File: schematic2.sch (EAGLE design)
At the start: 71 parts, among them IC6 DS3231/SO

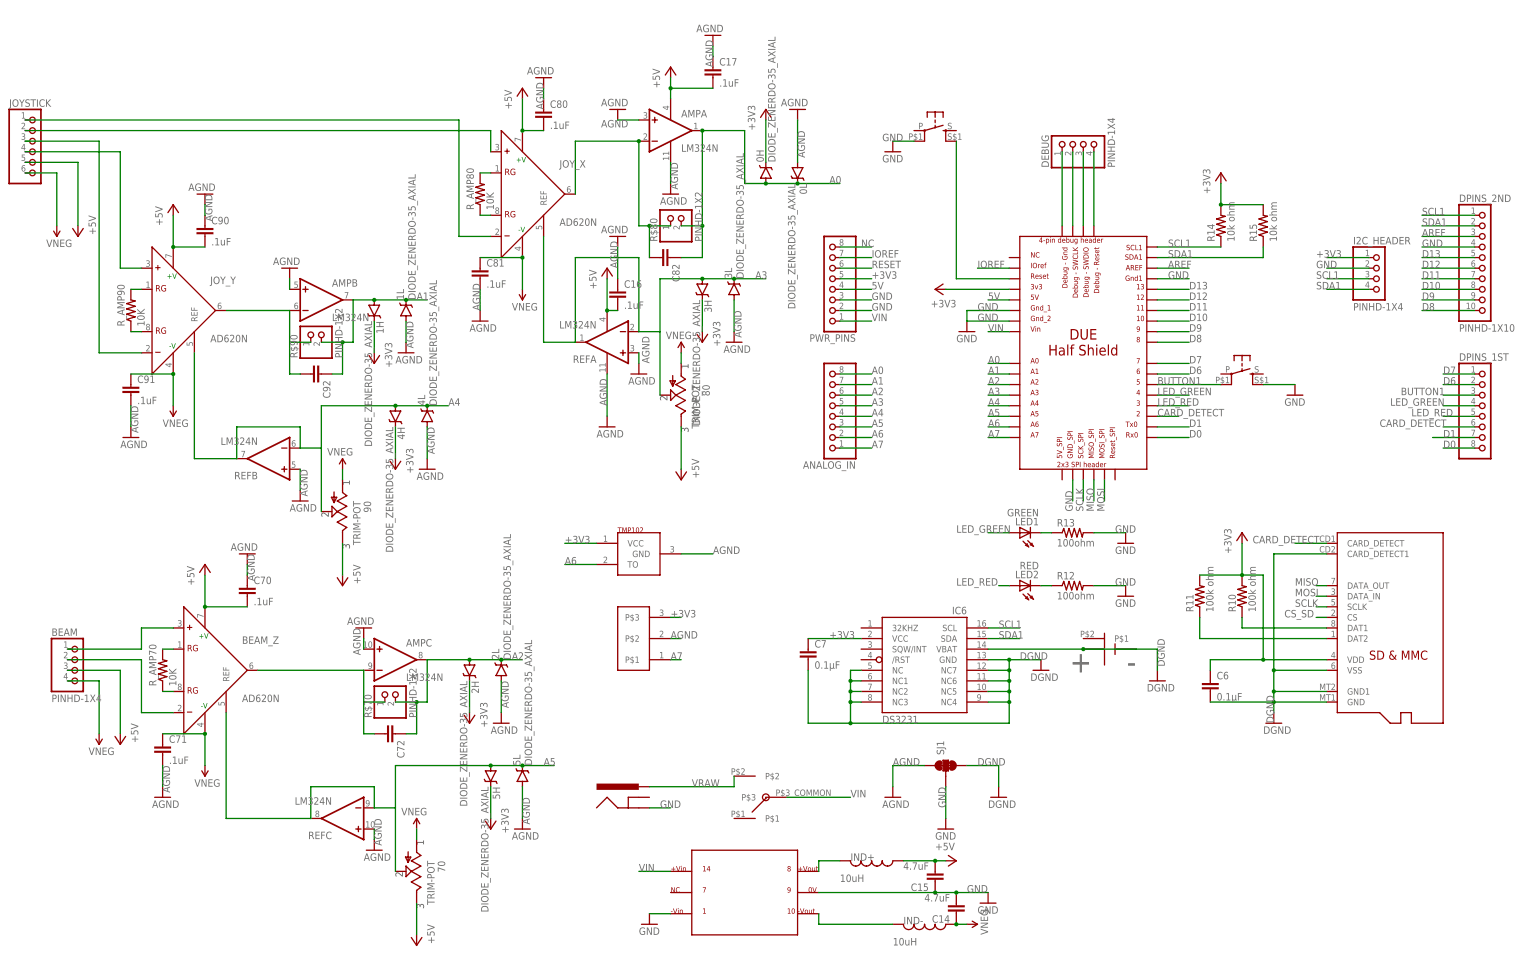
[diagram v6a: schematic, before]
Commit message: Fixed the RC filter arrangement on the 2nd stage op-amps for all three inputs. Move the adjust resistors (for 2nd stage amplification setting) in line with the signal line from the AD620s to the LM324s.
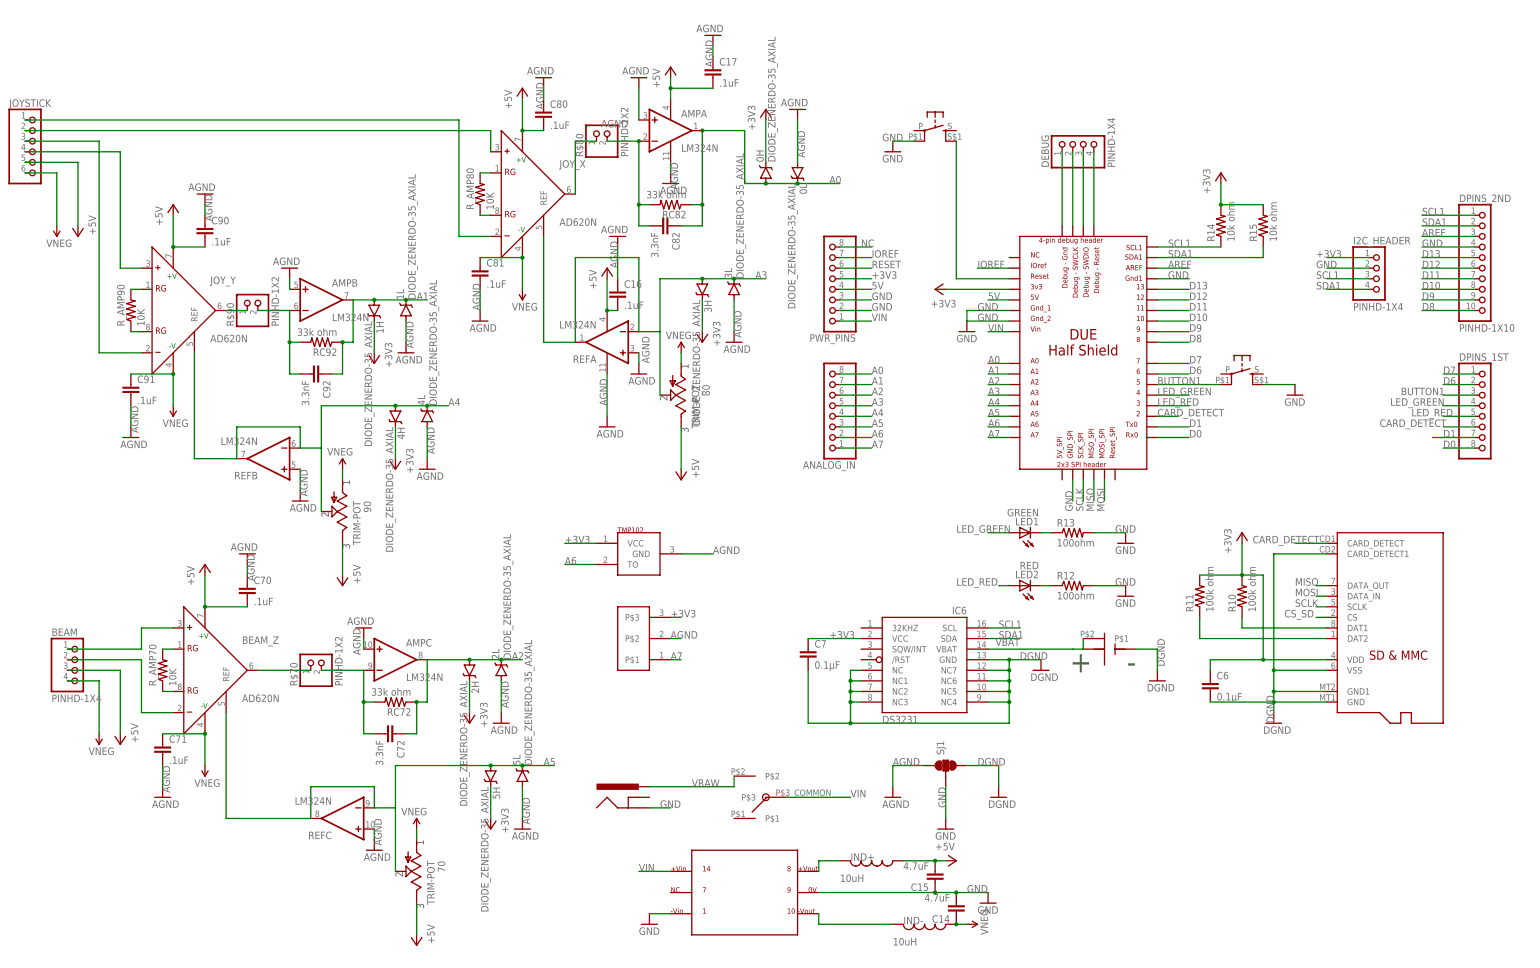
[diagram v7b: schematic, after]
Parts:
- added RC72, RC82, RC92: 33k ohm, Felicia_force_logger:RESISTOR_SMDR0805
- C72, C82, C92: value (none) -> 3.3nF
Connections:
- removed net N$26: IC6.VBAT, U$12.VBAT
- new net N$3: JOY_X.OUT, R$80.1
- new net N$4: BEAM_Z.OUT, R$70.1
- new net N$8: JOY_Y.OUT, R$90.1
- new net VBAT: IC6.VBAT, U$12.P$1, U$12.VBAT
- net A0: now also RC82.1; no longer R$80.2
- net A1: now also RC92.1; no longer R$90.2
- net A2: now also RC72.1; no longer R$70.2
- net N$11: now also R$80.2, RC82.2; no longer JOY_X.OUT, R$80.1
- net N$21: now also R$90.2, RC92.2; no longer JOY_Y.OUT, R$90.1
- net N$25: now also R$70.2, RC72.2; no longer BEAM_Z.OUT, R$70.1
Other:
- moved on the sheet: C82, R$70, R$80, R$90

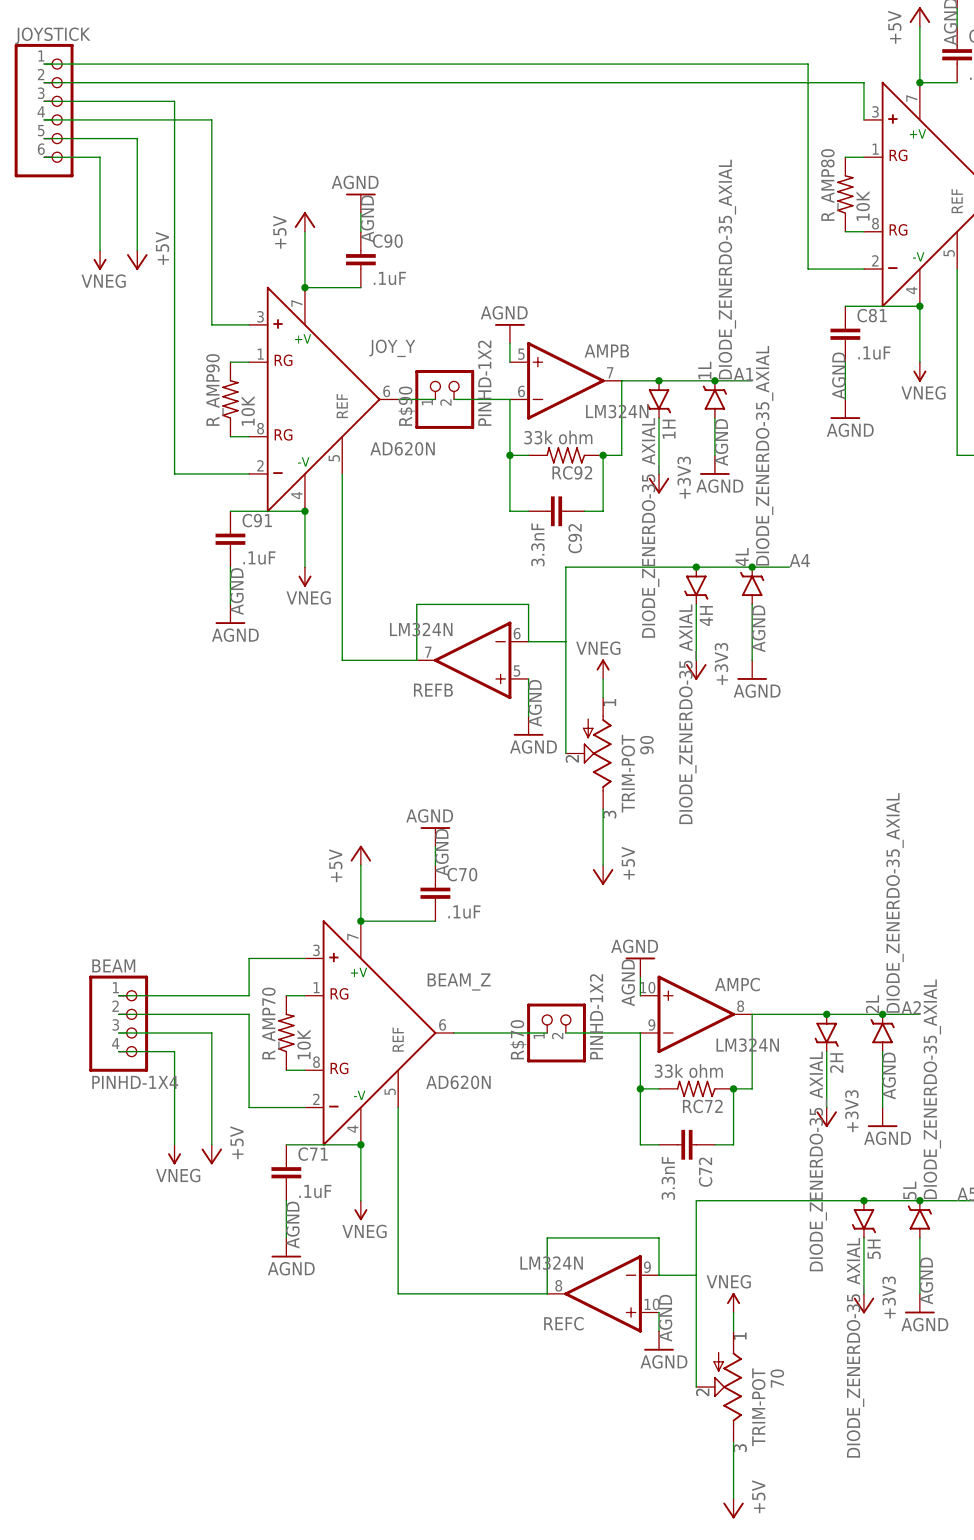
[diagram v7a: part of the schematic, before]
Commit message: Moved the amps around to try to minimize the rats nest. Moved all capacitors to the underside of the board, while all resistors and inductors remain on the top of the board. Added two mounting holes just for the hell of it.
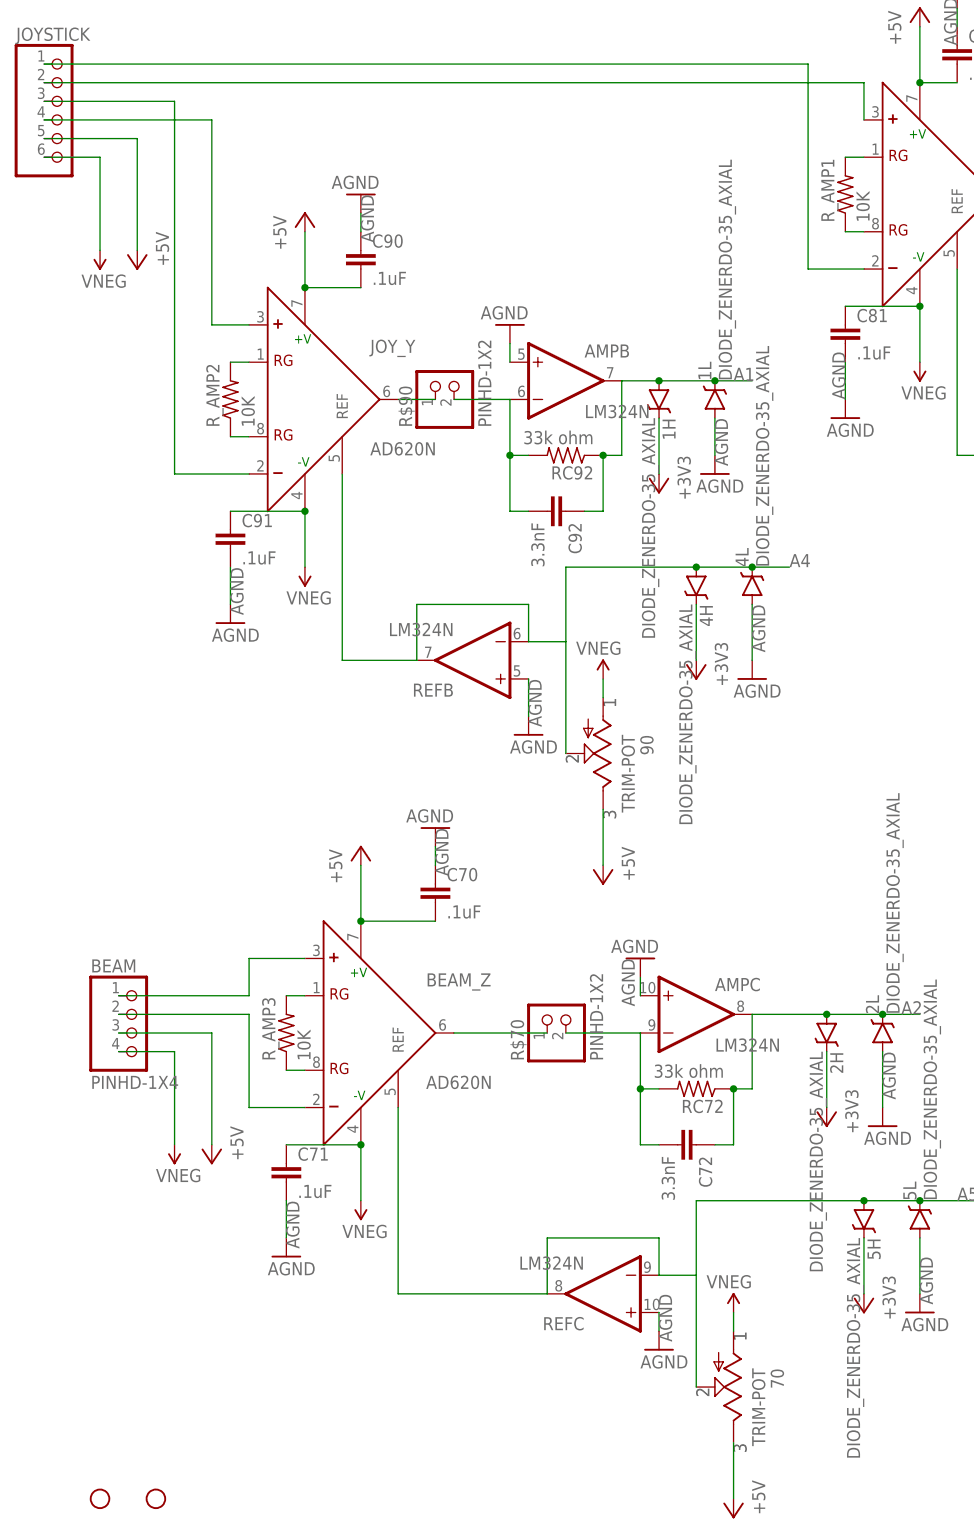
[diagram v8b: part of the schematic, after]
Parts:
- added STANDOFF1, STANDOFF2: STAND-OFF, miller:STAND-OFF
- renumbered R_AMP70 to R_AMP3, R_AMP80 to R_AMP1, R_AMP90 to R_AMP2
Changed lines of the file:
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@@
 <part name="C92" library="Felicia_force_logger" deviceset="CAP" device="0805" value="3.3nF"/>
 <part name="C82" library="Felicia_force_logger" deviceset="CAP" device="0805" value="3.3nF"/>
-<part name="R_AMP90" library="Felicia_force_logger" deviceset="RESISTOR_SMD" device="R0805" value="10K"/>
-<part name="R_AMP80" library="Felicia_force_logger" deviceset="RESISTOR_SMD" device="R0805" value="10K"/>
-<part name="R_AMP70" library="Felicia_force_logger" deviceset="RESISTOR_SMD" device="R0805" value="10K"/>
+<part name="R_AMP2" library="Felicia_force_logger" deviceset="RESISTOR_SMD" device="R0805" value="10K"/>
+<part name="R_AMP1" library="Felicia_force_logger" deviceset="RESISTOR_SMD" device="R0805" value="10K"/>
+<part name="R_AMP3" library="Felicia_force_logger" deviceset="RESISTOR_SMD" device="R0805" value="10K"/>
 <part name="U$3" library="Felicia_force_logger" deviceset="DC-DC_CONVERTER_DUAL_SUPPLY" device=""/>
 <part name="GND7" library="Felicia_force_logger" deviceset="GND" device=""/>
@@
 <part name="RC82" library="Felicia_force_logger" deviceset="RESISTOR_SMD" device="R0805" value="33k ohm"/>
 <part name="RC72" library="Felicia_force_logger" deviceset="RESISTOR_SMD" device="R0805" value="33k ohm"/>
+<part name="STANDOFF1" library="miller" deviceset="STAND-OFF" device=""/>
+<part name="STANDOFF2" library="miller" deviceset="STAND-OFF" device=""/>
 </parts>
 <sheets>
@@
 <instance part="C92" gate="G$1" x="66.04" y="139.7" rot="R270"/>
 <instance part="C82" gate="G$1" x="149.86" y="175.26" rot="R270"/>
-<instance part="R_AMP90" gate="G$1" x="22.86" y="154.94" rot="R90"/>
-<instance part="R_AMP80" gate="G$1" x="106.68" y="182.88" rot="R90"/>
-<instance part="R_AMP70" gate="G$1" x="30.48" y="68.58" rot="R90"/>
+<instance part="R_AMP2" gate="G$1" x="22.86" y="154.94" rot="R90"/>
+<instance part="R_AMP1" gate="G$1" x="106.68" y="182.88" rot="R90"/>
+<instance part="R_AMP3" gate="G$1" x="30.48" y="68.58" rot="R90"/>
 <instance part="U$3" gate="G$1" x="170.18" y="15.24"/>
 <instance part="GND7" gate="1" x="147.32" y="7.62"/>
@@
 <instance part="RC82" gate="G$1" x="152.4" y="180.34" rot="R180"/>
 <instance part="RC72" gate="G$1" x="86.36" y="60.96" rot="R180"/>
+<instance part="STANDOFF1" gate="G$1" x="5.08" y="5.08"/>
+<instance part="STANDOFF2" gate="G$1" x="12.7" y="5.08"/>
 </instances>
 <busses>
@@
 <pinref part="JOY_X" gate="G$1" pin="RG@1"/>
 <wire x1="106.68" y1="187.96" x2="109.22" y2="187.96" width="0.1524" layer="91"/>
-<pinref part="R_AMP80" gate="G$1" pin="2"/>
+<pinref part="R_AMP1" gate="G$1" pin="2"/>
 </segment>
 </net>
@@
 <pinref part="JOY_X" gate="G$1" pin="RG@2"/>
 <wire x1="106.68" y1="177.8" x2="109.22" y2="177.8" width="0.1524" layer="91"/>
-<pinref part="R_AMP80" gate="G$1" pin="1"/>
+<pinref part="R_AMP1" gate="G$1" pin="1"/>
 </segment>
 </net>
@@
 <pinref part="BEAM_Z" gate="G$1" pin="RG@1"/>
 <wire x1="30.48" y1="73.66" x2="33.02" y2="73.66" width="0.1524" layer="91"/>
-<pinref part="R_AMP70" gate="G$1" pin="2"/>
+<pinref part="R_AMP3" gate="G$1" pin="2"/>
 </segment>
 </net>
@@
 <pinref part="BEAM_Z" gate="G$1" pin="RG@2"/>
 <wire x1="30.48" y1="63.5" x2="33.02" y2="63.5" width="0.1524" layer="91"/>
-<pinref part="R_AMP70" gate="G$1" pin="1"/>
+<pinref part="R_AMP3" gate="G$1" pin="1"/>
 </segment>
 </net>
@@
 <segment>
 <pinref part="JOY_Y" gate="G$1" pin="RG@1"/>
-<pinref part="R_AMP90" gate="G$1" pin="2"/>
+<pinref part="R_AMP2" gate="G$1" pin="2"/>
 <wire x1="22.86" y1="160.02" x2="25.4" y2="160.02" width="0.1524" layer="91"/>
 </segment>
@@
 <segment>
 <pinref part="JOY_Y" gate="G$1" pin="RG@2"/>
-<pinref part="R_AMP90" gate="G$1" pin="1"/>
+<pinref part="R_AMP2" gate="G$1" pin="1"/>
 <wire x1="22.86" y1="149.86" x2="25.4" y2="149.86" width="0.1524" layer="91"/>
 </segment>
